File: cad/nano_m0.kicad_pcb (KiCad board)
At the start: 2 copper layers, 34.3 x 45.1 mm, 29 parts, among them J1 Conn_01x10, J2 Conn_01x10, J3 USB_B_Micro, J4 SWD, SW1 SW_SPST, SW2 SW_SPST, U1 AP2112K-3.3TRG1, U2 STM32F0706P6, Y1 16MHz

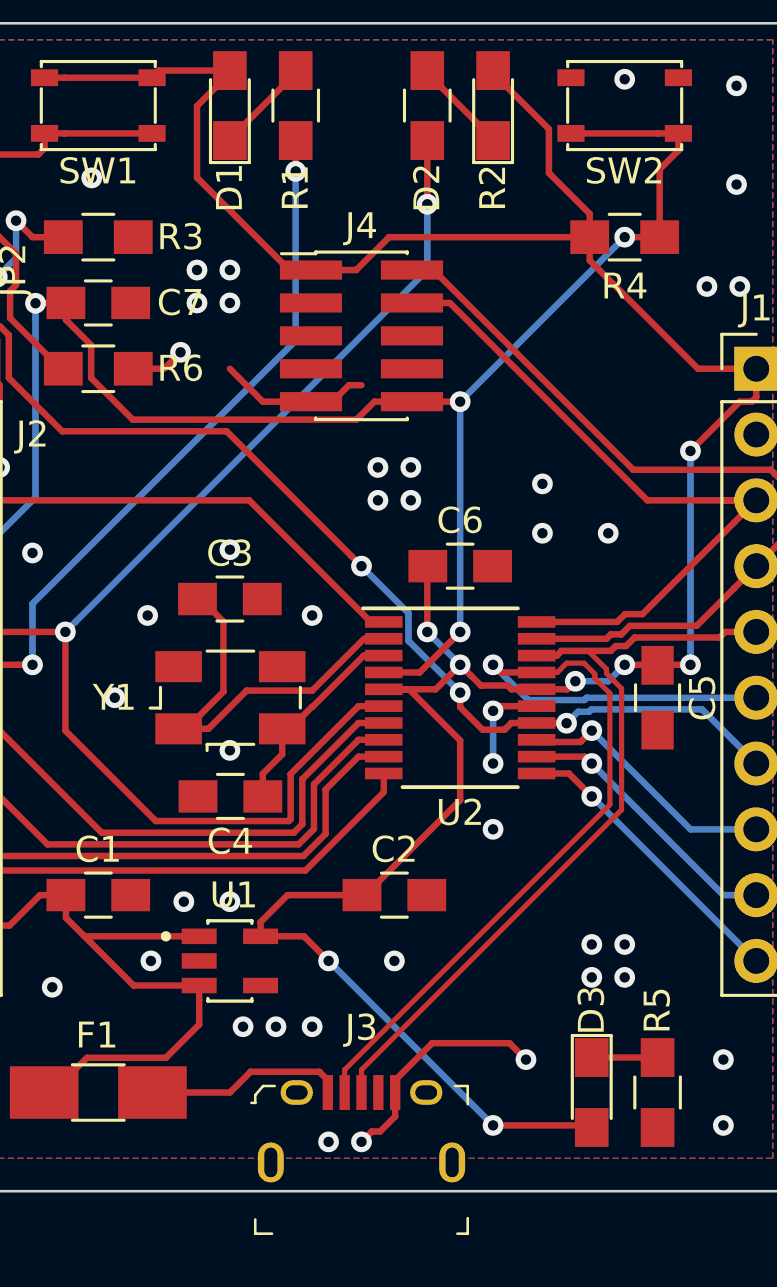
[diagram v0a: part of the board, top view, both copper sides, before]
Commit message: changes to crystal
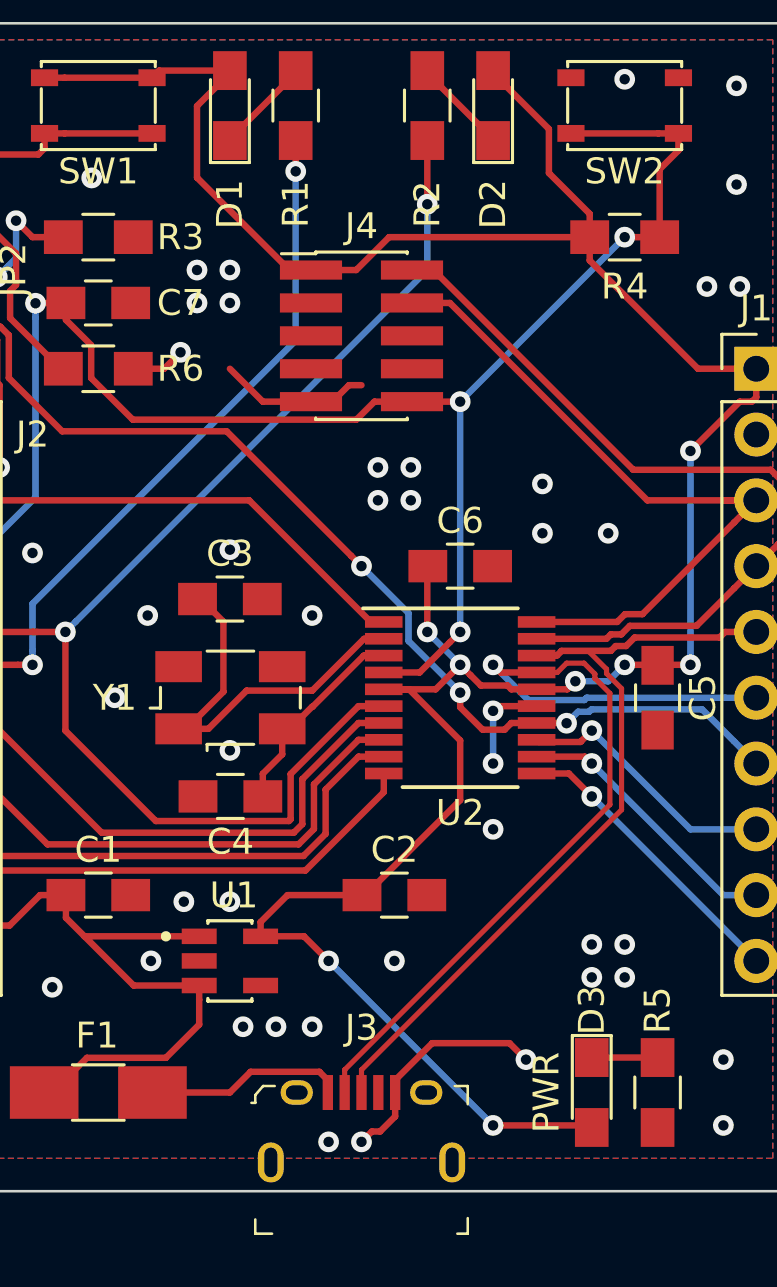
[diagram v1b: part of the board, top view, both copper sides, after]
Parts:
- D3: value LED -> PWR
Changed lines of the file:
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@@
   (page A4)
   (layers
-    (0 F.Cu signal hide)
+    (0 F.Cu signal)
     (31 B.Cu signal hide)
     (32 B.Adhes user)
@@
     (34 B.Paste user)
     (35 F.Paste user)
-    (36 B.SilkS user hide)
+    (36 B.SilkS user)
     (37 F.SilkS user)
     (38 B.Mask user)
@@
     (tags "resistor 0805")
     (attr smd)
-    (fp_text reference D1 (at -3.175 0 90) (layer F.SilkS)
+    (fp_text reference D1 (at -3.81 0 90) (layer F.SilkS)
       (effects (font (size 1 1) (thickness 0.15)))
     )
@@
     (tags "resistor 0805")
     (attr smd)
-    (fp_text reference D2 (at -3.175 -2.54 90) (layer F.SilkS)
+    (fp_text reference D2 (at -3.81 0 90) (layer F.SilkS)
       (effects (font (size 1 1) (thickness 0.15)))
     )
@@
     (tags "resistor 0805")
     (attr smd)
-    (fp_text reference R1 (at 3.175 0 270) (layer F.SilkS)
+    (fp_text reference R1 (at 3.81 0 270) (layer F.SilkS)
       (effects (font (size 1 1) (thickness 0.15)))
     )
@@
     (tags "resistor 0805")
     (attr smd)
-    (fp_text reference R2 (at 3.175 -2.54 270) (layer F.SilkS)
+    (fp_text reference R2 (at 3.81 0 270) (layer F.SilkS)
       (effects (font (size 1 1) (thickness 0.15)))
     )
@@
       (effects (font (size 1 1) (thickness 0.15)))
     )
-    (fp_text value LED (at 0 1.75 270) (layer F.Fab)
+    (fp_text value PWR (at 0 1.75 270) (layer F.SilkS)
       (effects (font (size 1 1) (thickness 0.15)))
     )
@@
   (segment (start 113.06 142.24) (end 113.06 143.165) (width 0.25) (layer F.Cu) (net 1) (status 10))
   (segment (start 104.14 114.3) (end 104.775 113.665) (width 0.25) (layer F.Cu) (net 1))
-  (segment (start 102.95 114.3) (end 104.14 114.3) (width 0.25) (layer F.Cu) (net 1))
+  (segment (start 102.95 114.3) (end 104.14 114.3) (width 0.25) (layer F.Cu) (net 1) (status 10))
   (segment (start 95.42 114.3) (end 95.25 114.47) (width 0.25) (layer F.Cu) (net 2))
   (segment (start 96.52 114.3) (end 95.42 114.3) (width 0.25) (layer F.Cu) (net 2) (status 10))
@@
   (segment (start 115.169979 124.859999) (end 115.569978 124.46) (width 0.25) (layer F.Cu) (net 6))
   (segment (start 99.187266 111.76) (end 99.175669 111.771597) (width 0.25) (layer F.Cu) (net 6))
-  (segment (start 100.35 111.76) (end 99.187266 111.76) (width 0.25) (layer F.Cu) (net 6))
+  (segment (start 100.35 111.76) (end 99.187266 111.76) (width 0.25) (layer F.Cu) (net 6) (status 10))
   (segment (start 99.175669 119.264331) (end 99.175669 112.337282) (width 0.25) (layer B.Cu) (net 6))
   (via (at 99.175669 111.771597) (size 0.8) (drill 0.4) (layers F.Cu B.Cu) (net 6))
   (segment (start 99.175669 112.337282) (end 99.175669 111.771597) (width 0.25) (layer B.Cu) (net 6))
-  (segment (start 96.52 121.92) (end 99.175669 119.264331) (width 0.25) (layer B.Cu) (net 6))
-  (segment (start 100.35 112.414998) (end 100.35 111.76) (width 0.25) (layer F.Cu) (net 6))
+  (segment (start 96.52 121.92) (end 99.175669 119.264331) (width 0.25) (layer B.Cu) (net 6) (status 10))
+  (segment (start 100.35 112.414998) (end 100.35 111.76) (width 0.25) (layer F.Cu) (net 6) (status 20))
   (segment (start 101.325001 113.389999) (end 100.35 112.414998) (width 0.25) (layer F.Cu) (net 6))
   (segment (start 102.929999 116.265001) (end 101.325001 114.660003) (width 0.25) (layer F.Cu) (net 6))
@@
   (segment (start 111.564999 116.265001) (end 102.929999 116.265001) (width 0.25) (layer F.Cu) (net 6))
   (segment (start 112.26 115.57) (end 111.564999 116.265001) (width 0.25) (layer F.Cu) (net 6))
-  (segment (start 113.71 115.57) (end 112.26 115.57) (width 0.25) (layer F.Cu) (net 6))
+  (segment (start 113.71 115.57) (end 112.26 115.57) (width 0.25) (layer F.Cu) (net 6) (status 10))
   (segment (start 106.68 105.43) (end 106.68 105.49) (width 0.25) (layer F.Cu) (net 7) (status 30))
   (segment (start 109.22 102.89) (end 106.68 105.43) (width 0.25) (layer F.Cu) (net 7) (status 30))
@@
   (segment (start 117.286998 128.233002) (end 117.545 127.975) (width 0.25) (layer F.Cu) (net 14))
   (segment (start 117.545 127.975) (end 118.52 127.975) (width 0.25) (layer F.Cu) (net 14) (status 20))
-  (segment (start 96.46499 111.19501) (end 96.46499 112.151401) (width 0.25) (layer F.Cu) (net 14))
+  (segment (start 96.46499 111.19501) (end 96.46499 112.151401) (width 0.25) (layer F.Cu) (net 14) (status 10))
   (segment (start 97.816402 112.67499) (end 98.145011 113.003599) (width 0.25) (layer F.Cu) (net 14))
   (segment (start 98.145012 114.655011) (end 100.205011 116.715011) (width 0.25) (layer F.Cu) (net 14))
   (segment (start 111.360001 121.520001) (end 111.76 121.92) (width 0.25) (layer F.Cu) (net 14))
   (segment (start 96.988578 112.674989) (end 97.816402 112.67499) (width 0.25) (layer F.Cu) (net 14))
-  (segment (start 96.52 111.14) (end 96.46499 111.19501) (width 0.25) (layer F.Cu) (net 14))
+  (segment (start 96.52 111.14) (end 96.46499 111.19501) (width 0.25) (layer F.Cu) (net 14) (status 30))
   (segment (start 106.555011 116.715011) (end 111.360001 121.520001) (width 0.25) (layer F.Cu) (net 14))
   (segment (start 96.46499 112.151401) (end 96.988578 112.674989) (width 0.25) (layer F.Cu) (net 14))
@@
   (segment (start 100.205011 116.715011) (end 106.555011 116.715011) (width 0.25) (layer F.Cu) (net 14))
   (segment (start 99.06 109.22) (end 98.425012 108.585012) (width 0.25) (layer F.Cu) (net 14))
-  (segment (start 100.25 109.22) (end 99.06 109.22) (width 0.25) (layer F.Cu) (net 14))
+  (segment (start 100.25 109.22) (end 99.06 109.22) (width 0.25) (layer F.Cu) (net 14) (status 10))
   (via (at 98.425 108.585012) (size 0.8) (drill 0.4) (layers F.Cu B.Cu) (net 14))
   (segment (start 98.425012 108.585012) (end 98.425 108.585012) (width 0.25) (layer F.Cu) (net 14))
@@
   (segment (start 97.69999 110.96001) (end 97.69999 110.758464) (width 0.25) (layer F.Cu) (net 14))
   (segment (start 98.099989 110.358465) (end 97.69999 110.758464) (width 0.25) (layer B.Cu) (net 14))
-  (segment (start 96.52 111.14) (end 97.52 111.14) (width 0.25) (layer F.Cu) (net 14))
+  (segment (start 96.52 111.14) (end 97.52 111.14) (width 0.25) (layer F.Cu) (net 14) (status 10))
   (via (at 97.69999 110.758464) (size 0.8) (drill 0.4) (layers F.Cu B.Cu) (net 14))
   (via (at 120.65 128.27) (size 0.8) (drill 0.4) (layers F.Cu B.Cu) (net 15))
@@
   (segment (start 97.722081 119.38) (end 96.52 119.38) (width 0.25) (layer F.Cu) (net 23) (status 20))
   (segment (start 112.12 124.075) (end 107.425 119.38) (width 0.25) (layer F.Cu) (net 23) (status 10))
-  (segment (start 96.52 108.08) (end 96.52 107.33) (width 0.25) (layer F.Cu) (net 23))
+  (segment (start 96.52 108.08) (end 96.52 107.33) (width 0.25) (layer F.Cu) (net 23) (status 20))
   (segment (start 97.025 108.585) (end 96.52 108.08) (width 0.25) (layer F.Cu) (net 23))
   (segment (start 97.155 108.585) (end 97.025 108.585) (width 0.25) (layer F.Cu) (net 23))
   (segment (start 98.425 109.855) (end 97.155 108.585) (width 0.25) (layer F.Cu) (net 23))
   (segment (start 98.425 111.067318) (end 98.425 109.855) (width 0.25) (layer F.Cu) (net 23))
-  (segment (start 100.25 114.3) (end 100.15 114.3) (width 0.25) (layer F.Cu) (net 23))
+  (segment (start 100.25 114.3) (end 100.15 114.3) (width 0.25) (layer F.Cu) (net 23) (status 30))
   (segment (start 98.194498 112.344498) (end 98.194498 111.29782) (width 0.25) (layer F.Cu) (net 23))
-  (segment (start 100.15 114.3) (end 98.194498 112.344498) (width 0.25) (layer F.Cu) (net 23))
+  (segment (start 100.15 114.3) (end 98.194498 112.344498) (width 0.25) (layer F.Cu) (net 23) (status 10))
   (segment (start 98.194498 111.29782) (end 98.425 111.067318) (width 0.25) (layer F.Cu) (net 23))
   (segment (start 96.52 108.08) (end 96.299999 107.859999) (width 0.25) (layer F.Cu) (net 23))
@@
   (segment (start 95.159999 107.405001) (end 95.235 107.33) (width 0.25) (layer F.Cu) (net 23))
   (segment (start 97.630001 113.124999) (end 96.069989 113.124999) (width 0.25) (layer F.Cu) (net 23))
-  (segment (start 95.235 107.33) (end 96.52 107.33) (width 0.25) (layer F.Cu) (net 23))
+  (segment (start 95.235 107.33) (end 96.52 107.33) (width 0.25) (layer F.Cu) (net 23) (status 20))
   (segment (start 97.79 114.93641) (end 97.695001 114.841411) (width 0.25) (layer F.Cu) (net 23))
   (segment (start 95.159999 112.215009) (end 95.159999 107.405001) (width 0.25) (layer F.Cu) (net 23))
@@
   (segment (start 96.52 106.03) (end 96.52 106.504999) (width 0.25) (layer F.Cu) (net 24) (status 30))
   (via (at 95.26501 106.03) (size 0.8) (drill 0.4) (layers F.Cu B.Cu) (net 24))
-  (segment (start 96.52 106.03) (end 95.26501 106.03) (width 0.25) (layer F.Cu) (net 24))
+  (segment (start 96.52 106.03) (end 95.26501 106.03) (width 0.25) (layer F.Cu) (net 24) (status 10))
   (segment (start 95.26501 107.96501) (end 95.885 108.585) (width 0.25) (layer B.Cu) (net 24))
   (via (at 95.885 108.585) (size 0.8) (drill 0.4) (layers F.Cu B.Cu) (net 24))
   (segment (start 95.26501 106.03) (end 95.26501 107.96501) (width 0.25) (layer B.Cu) (net 24))
-  (segment (start 95.885 109.205) (end 96.52 109.84) (width 0.25) (layer F.Cu) (net 24))
+  (segment (start 95.885 109.205) (end 96.52 109.84) (width 0.25) (layer F.Cu) (net 24) (status 20))
   (segment (start 95.885 108.585) (end 95.885 109.205) (width 0.25) (layer F.Cu) (net 24))
   (segment (start 123.19 140.89) (end 120.65 140.89) (width 0.25) (layer F.Cu) (net 25) (status 30))

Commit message: board v2
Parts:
- removed the REF*** at (120.0, 108.6)
- added REF***: OSHW-Symbol_6.7x6mm_SilkScreen, Symbols:OSHW-Symbol_6.7x6mm_SilkScreen, B.Cu at (143.3, 72.6)
- C3, C4: value 15pF -> 22pF
- C7, F1, JP1, JP2, R3, R4, R6: moved to B.Cu
- U1: value AP2112K-3.3TRG1 -> (none)
- Y1: value 16MHz -> Crystal; footprint Crystals:Crystal_SMD_Abracon_ABM3B-4pin_5.0x3.2mm -> Crystals:Crystal_SMD_SeikoEpson_TSX3225-4pin_3.2x2.5mm_HandSoldering
- moved F1 80.9 mm to (151.8, 78.7), turned to 270 degrees
- moved J3 79.9 mm to (151.8, 73.0), turned to 180 degrees
- moved D3 73.9 mm to (142.9, 71.8), turned to 0 degrees
- moved C1 72.4 mm to (146.1, 77.5), turned to 180 degrees
- moved R5 70.1 mm to (142.9, 74.9), turned to 0 degrees
- moved U1 68.4 mm to (146.1, 81.3)
- moved C4 66.9 mm to (156.0, 85.6)
- moved J2 65.9 mm to (161.3, 102.2), turned to 180 degrees
- moved C2 65.2 mm to (150.5, 81.3), turned to 270 degrees
- moved Y1 61.6 mm to (156.0, 90.1), turned to 90 degrees
- moved C3 57.0 mm to (156.0, 94.6), turned to 180 degrees
- moved C7 54.2 mm to (154.9, 102.2), turned to 270 degrees
- moved JP2 50.7 mm to (145.4, 97.0), turned to 0 degrees
- moved JP1 49.4 mm to (145.4, 99.6), turned to 0 degrees
- moved U2 48.5 mm to (147.7, 90.7), turned to 180 degrees
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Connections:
- C1 pad 1: +5V -> Net-(C1-Pad1)
- F1 pad 1: +5V -> Net-(C1-Pad1)
- F1 pad 2: VBUS -> +5V
- J2 pad 3: /BOOT -> /NRST
- J2 pad 4: /NRST -> /BOOT
- J3 pad 1: VBUS -> +5V
- U1 pad 1: +5V -> Net-(C1-Pad1)
- U1 pad 3: +5V -> Net-(C1-Pad1)
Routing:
- net +3V3: track 108.4 -> 81.0 mm, vias 8 -> 2
- net /PB1: track 47.4 -> 24.1 mm, vias 5 -> 2
- net /PA0: track 49.2 -> 28.4 mm
- net /PA1: track 48.5 -> 28.5 mm
- net /NRST: track 62.2 -> 42.6 mm, vias 4 -> 2
- net /BOOT: track 43.1 -> 25.2 mm
- net /PA13: track 31.1 -> 14.9 mm, vias 0 -> 2
- net Net-(C1-Pad1): track 0.00 -> 14.1 mm, vias 0 -> 2
- net /PA14: track 28.1 -> 16.5 mm, vias 0 -> 2
- net +5V: track 47.9 -> 38.1 mm, vias 0 -> 3
- net VBUS: track 7.71 -> 0.00 mm
- net /USB_N: track 35.8 -> 30.3 mm, vias 1 -> 2
- net /PA2: track 20.1 -> 14.8 mm
- net /PA3: track 19.1 -> 13.9 mm
- net /PA4: track 18.5 -> 13.5 mm
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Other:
- board size 34.3 x 45.1 mm -> 24.1 x 41.3 mm
- net class POWER added: clearance 0.25, trace_width 0.3, via_dia 0.8, via_drill 0.4
- board text added: "3.3V"
- board text added: "5V"
- board text added: "BOOT"
- board text added: "GND"
- board text added: "NANO-M0 @ZKLAPOW"
- board text added: "PA0"
- board text added: "PA1"
- board text added: "PA13"
- board text added: "PA14"
- board text added: "PA2"
- board text added: "PA3"
- board text added: "PA4"
- board text added: "PA5"
- board text added: "PA6"
- board text added: "PA7"
- board text added: "PB1"
- board text added: "RST"
- board text added: "USB_N"
- board text added: "USB_P"
- board text added: "V2"
- board text removed: "@zklapow"
- board text removed: "NANO-M0"
- board text removed: "V1"

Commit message: final v3 board
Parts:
- removed JP1: Jumper_NC_Small, Jumper:SolderJumper-2_P1.3mm_Bridged_Pad1.0x1.5mm
- removed JP2: Jumper_NO_Small, Jumper:SolderJumper-2_P1.3mm_Open_Pad1.0x1.5mm
- removed REF***: OSHW-Symbol_6.7x6mm_SilkScreen, Symbols:OSHW-Symbol_6.7x6mm_SilkScreen
- C1, C2, C3, C4, C5, C6: footprint Capacitors_SMD:C_0805_HandSoldering -> Capacitors_SMD:C_0805
- C7: footprint Capacitors_SMD:C_0805_HandSoldering -> Capacitors_SMD:C_0805; moved to F.Cu
- D1, D2, D3: footprint LEDs:LED_0805_HandSoldering -> LEDs:LED_0805
- F1: moved to F.Cu
- R1, R2, R5: value 80ohm -> 100; footprint Resistors_SMD:R_0805_HandSoldering -> Resistors_SMD:R_0805
- R3, R4, R6: footprint Resistors_SMD:R_0805_HandSoldering -> Resistors_SMD:R_0805; moved to F.Cu
- U1: value (none) -> AP2112K-3.3TRG1
- Y1: footprint Crystals:Crystal_SMD_SeikoEpson_TSX3225-4pin_3.2x2.5mm_HandSoldering -> Crystals:Crystal_SMD_SeikoEpson_TSX3225-4pin_3.2x2.5mm
- moved J2 52.5 mm to (114.3, 78.7), turned to 0 degrees
- moved SW2 43.5 mm to (116.5, 108.2)
- moved R2 43.0 mm to (119.5, 83.0), turned to 0 degrees
- moved D2 39.5 mm to (119.5, 85.5), turned to 0 degrees
- moved R4 36.5 mm to (121.5, 108.2)
- moved R1 36.0 mm to (119.5, 88.0), turned to 0 degrees
- moved F1 35.5 mm to (117.6, 69.1), turned to 180 degrees
- moved R6 33.8 mm to (119.5, 80.5), turned to 180 degrees
- moved D1 32.4 mm to (119.6, 90.5), turned to 0 degrees
- moved C4 31.8 mm to (124.9, 92.7), turned to 270 degrees
- moved C7 31.0 mm to (124.5, 108.2), turned to 90 degrees
- moved C1 30.3 mm to (116.1, 72.6)
- moved Y1 27.4 mm to (128.7, 92.6), turned to 180 degrees
- moved U1 26.0 mm to (120.7, 75.6)
- moved J3 25.3 mm to (127.0, 67.9)
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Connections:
- SW1 pad 2: Net-(JP1-Pad1) -> /PB1
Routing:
- net +3V3: track 81.0 -> 129.3 mm, vias 2 -> 8
- net /PA14: track 16.5 -> 34.5 mm, vias 2 -> 1
- net Net-(JP1-Pad1): track 17.5 -> 0.00 mm, vias 1 -> 0
- net /PA13: track 14.9 -> 31.3 mm, vias 2 -> 1
- net GND: track 25.3 -> 10.0 mm, vias 20 -> 52
- net /PA1: track 28.5 -> 14.1 mm, vias 2 -> 0
- net +5V: track 38.1 -> 25.5 mm, vias 3 -> 0
- net /PB1: track 24.1 -> 34.7 mm, vias 2 -> 0
- net /NRST: track 42.6 -> 52.5 mm
- net /PA7: track 6.78 -> 13.6 mm
- net /PA6: track 8.67 -> 15.5 mm
- net /PA5: track 9.99 -> 16.8 mm
- net /BOOT: track 25.2 -> 18.4 mm, vias 1 -> 0
- net /PA0: track 28.4 -> 22.7 mm, vias 2 -> 1
- net /PA4: track 13.5 -> 16.5 mm
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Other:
- board size 24.1 x 41.3 mm -> 30.5 x 48.3 mm
- net class 5v added: clearance 0.2, trace_width 0.35, via_dia 0.8, via_drill 0.4
- net class POWER removed
- board text added: "@ZKLAPOW"
- board text added: "NANO-M0"
- board text added: "RESET"
- board text added: "V3"
- board text removed: "3.3V"
- board text removed: "5V"
- board text removed: "BOOT"
- board text removed: "GND"
- board text removed: "NANO-M0 @ZKLAPOW"
- board text removed: "PA0"
- board text removed: "PA1"
- board text removed: "PA13"
- board text removed: "PA14"
- board text removed: "PA2"
- board text removed: "PA3"
- board text removed: "PA4"
- board text removed: "PA5"
- board text removed: "PA6"
- board text removed: "PA7"
- board text removed: "PB1"
- board text removed: "RST"
- board text removed: "USB_N"
- board text removed: "USB_P"
- board text removed: "V2"
